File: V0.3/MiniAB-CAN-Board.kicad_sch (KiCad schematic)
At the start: 119 parts, among them J1 PC-FAN, J10 USB_B_Micro, J11 ENDSTOP1, J12 CAN, J13 ENDSTOP2, J14 PROBE, J2 PC-FAN, J3 HE-FAN, J4 TH0, J5 H0, J6 STEPPER, J7 NEOPIXEL, J8 I2C, J9 Conn_02x03_Top_Bottom, Q1 AO3400A, Q2 AO3400A, Q3 AON7418, U1 ADXL345BCCZ-RL7, U2 STM32F103C8Tx, U3 74LVC1G17, U4 LP5907MFX-3.3, U5 TMC2209-LA, U6 TPS54202DDC, U7 TCAN330, Y1 8MHz

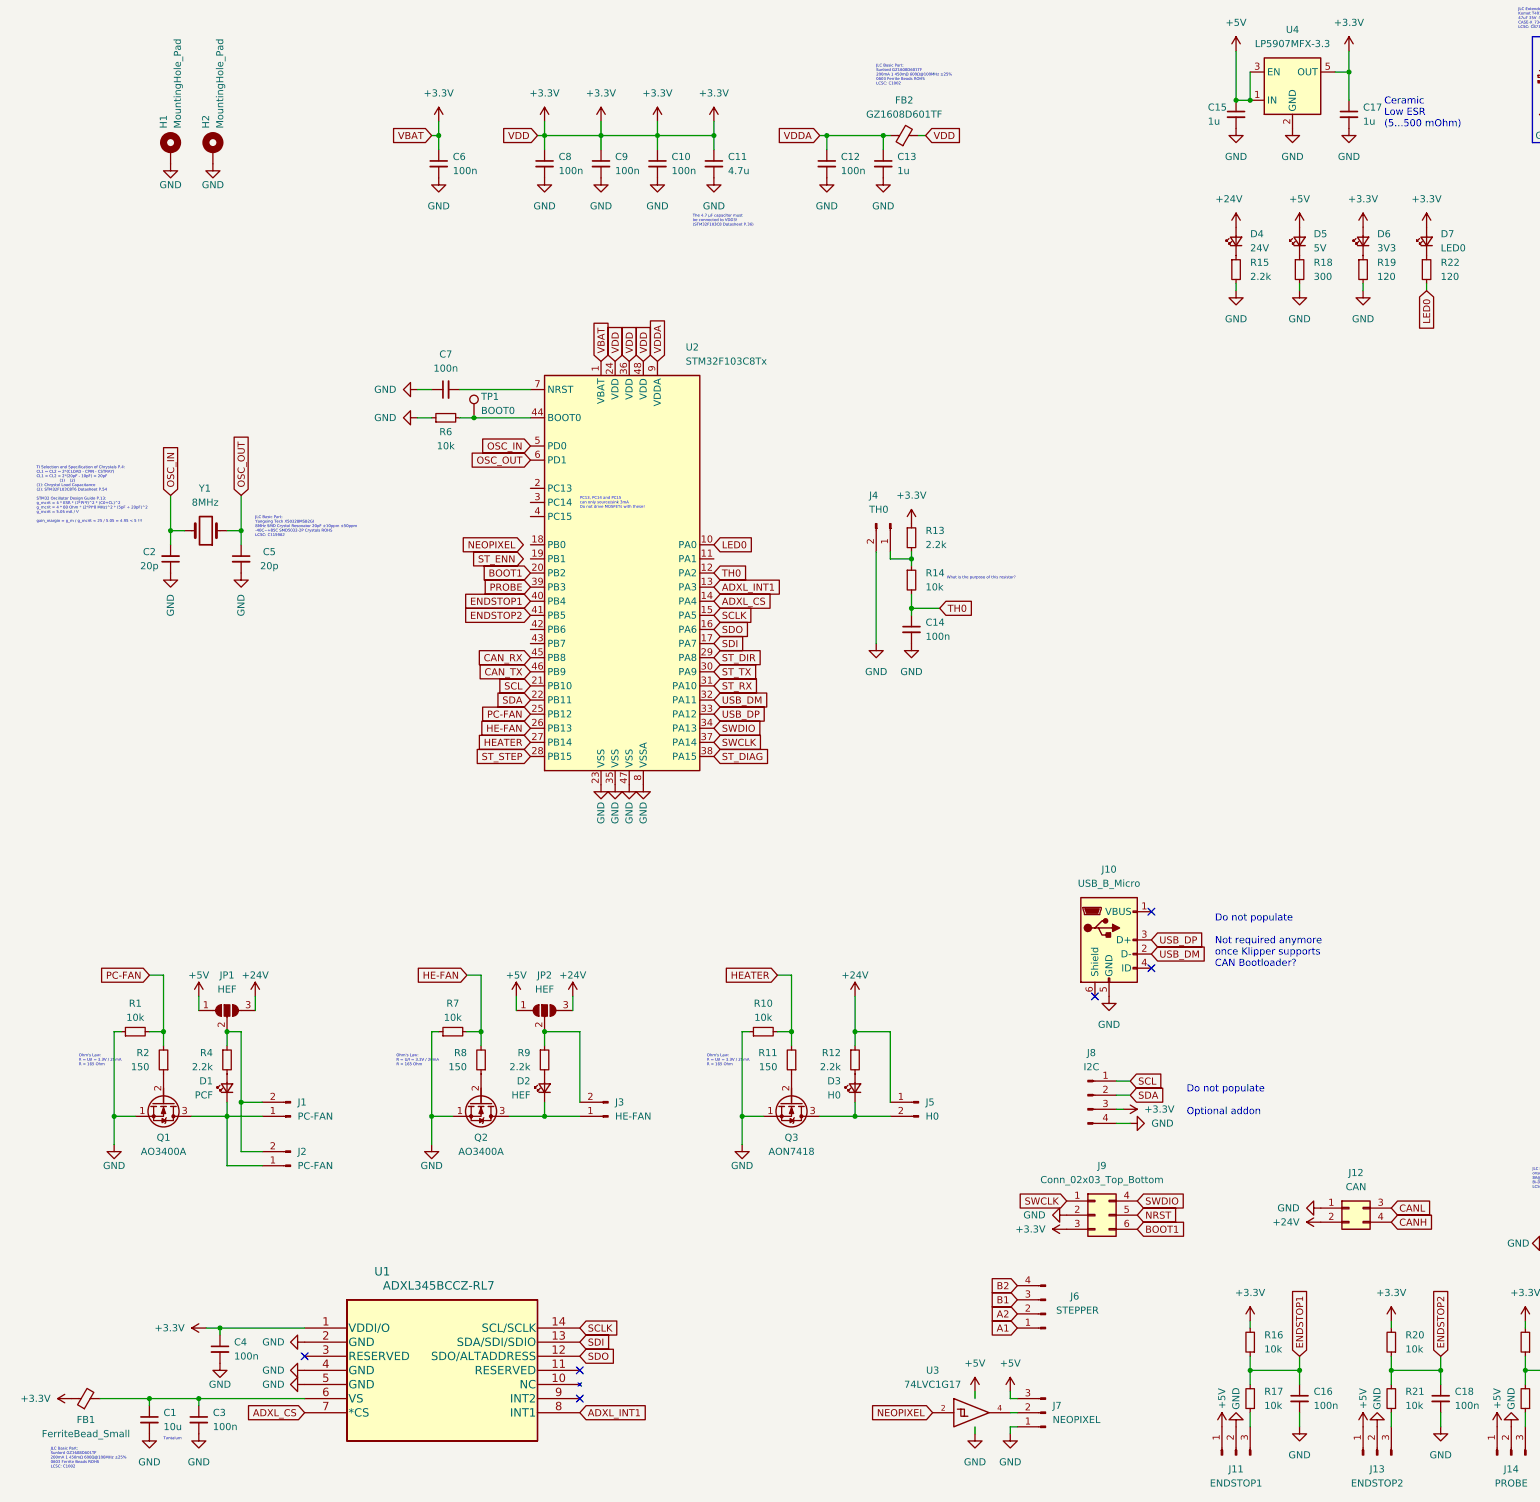
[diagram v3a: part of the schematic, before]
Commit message: Updated footprints to 0402 if possible
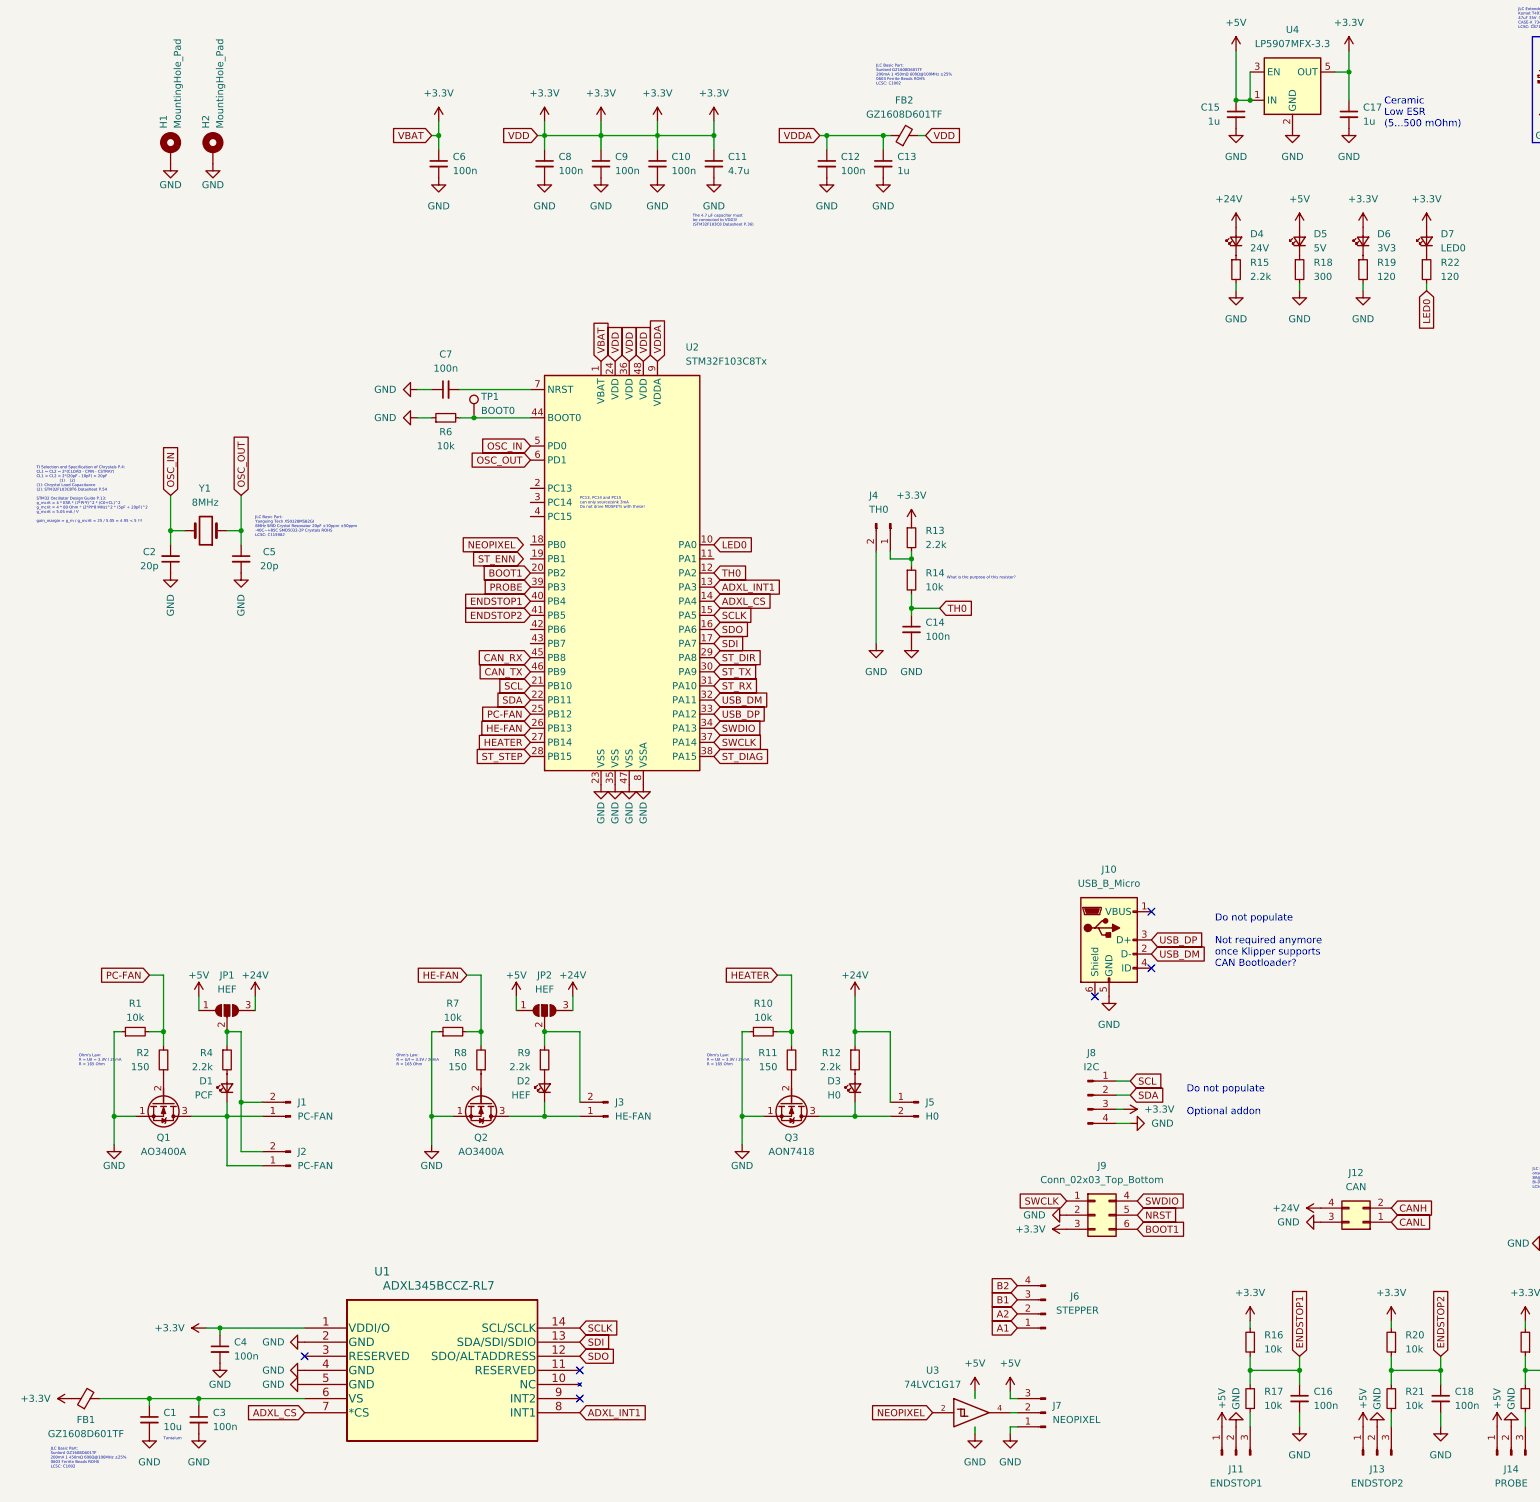
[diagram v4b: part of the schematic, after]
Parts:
- C10, C11, C12, C13, C14, C15, C16, C17, C18, C2, C20, C22, C23, C24, C26, C27, C28, C29, C3, C30, C33, C34, C35, C4, C40, C41, C43, C5, C6, C7, C8, C9: footprint Capacitor_SMD:C_0603_1608Metric -> Capacitor_SMD:C_0402_1005Metric
- D1, D2, D3, D4, D5, D6, D7: footprint LED_SMD:LED_0805_2012Metric -> LED_SMD:LED_0402_1005Metric
- D9: footprint LED_SMD:LED_0603_1608Metric -> LED_SMD:LED_0402_1005Metric
- FB1: value FerriteBead_Small -> GZ1608D601TF
- R1, R10, R11, R12, R13, R14, R15, R16, R17, R18, R19, R2, R20, R21, R22, R23, R24, R25, R26, R29, R34, R35, R36, R4, R6, R7, R8, R9: footprint Resistor_SMD:R_0603_1608Metric -> Resistor_SMD:R_0402_1005Metric
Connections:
- net +24V: now also J12.4 (Pin_4); no longer J12.2 (Pin_2)
- net CANH: now also J12.2 (Pin_2); no longer J12.4 (Pin_4)
- net CANL: now also J12.1 (Pin_1); no longer J12.3 (Pin_3)
- net GND: now also J12.3 (Pin_3); no longer J12.1 (Pin_1)
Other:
- moved on the sheet: J12

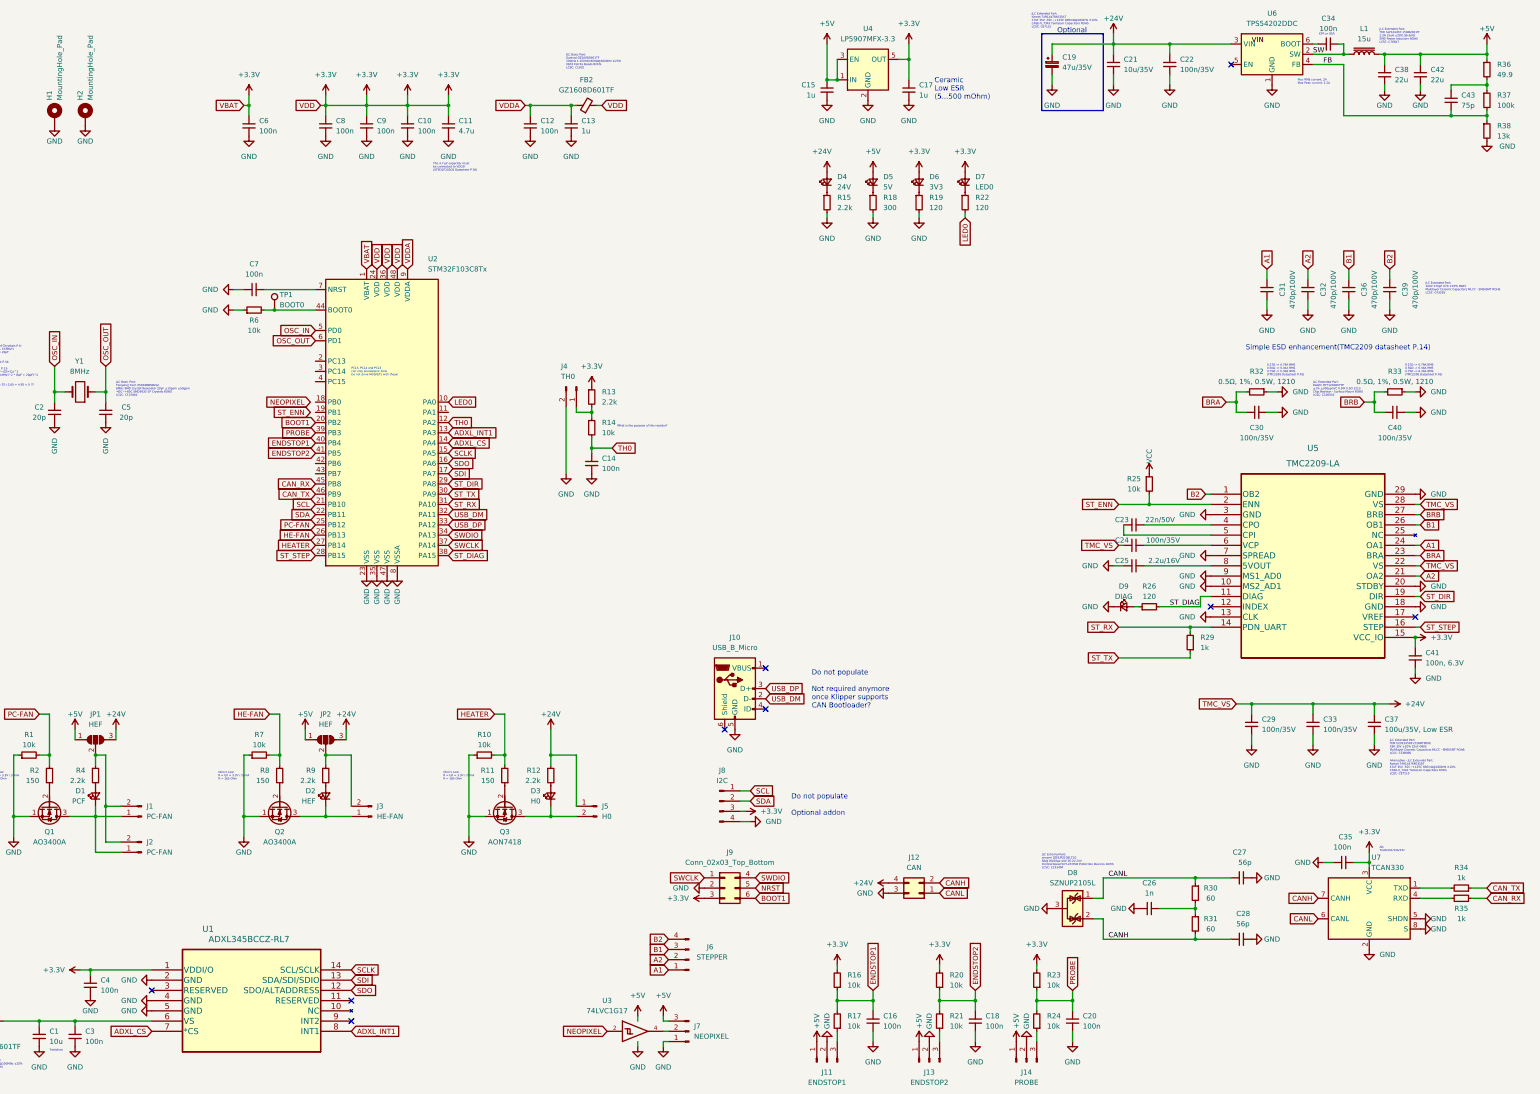
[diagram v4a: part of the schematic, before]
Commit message: TMC added to V0.3
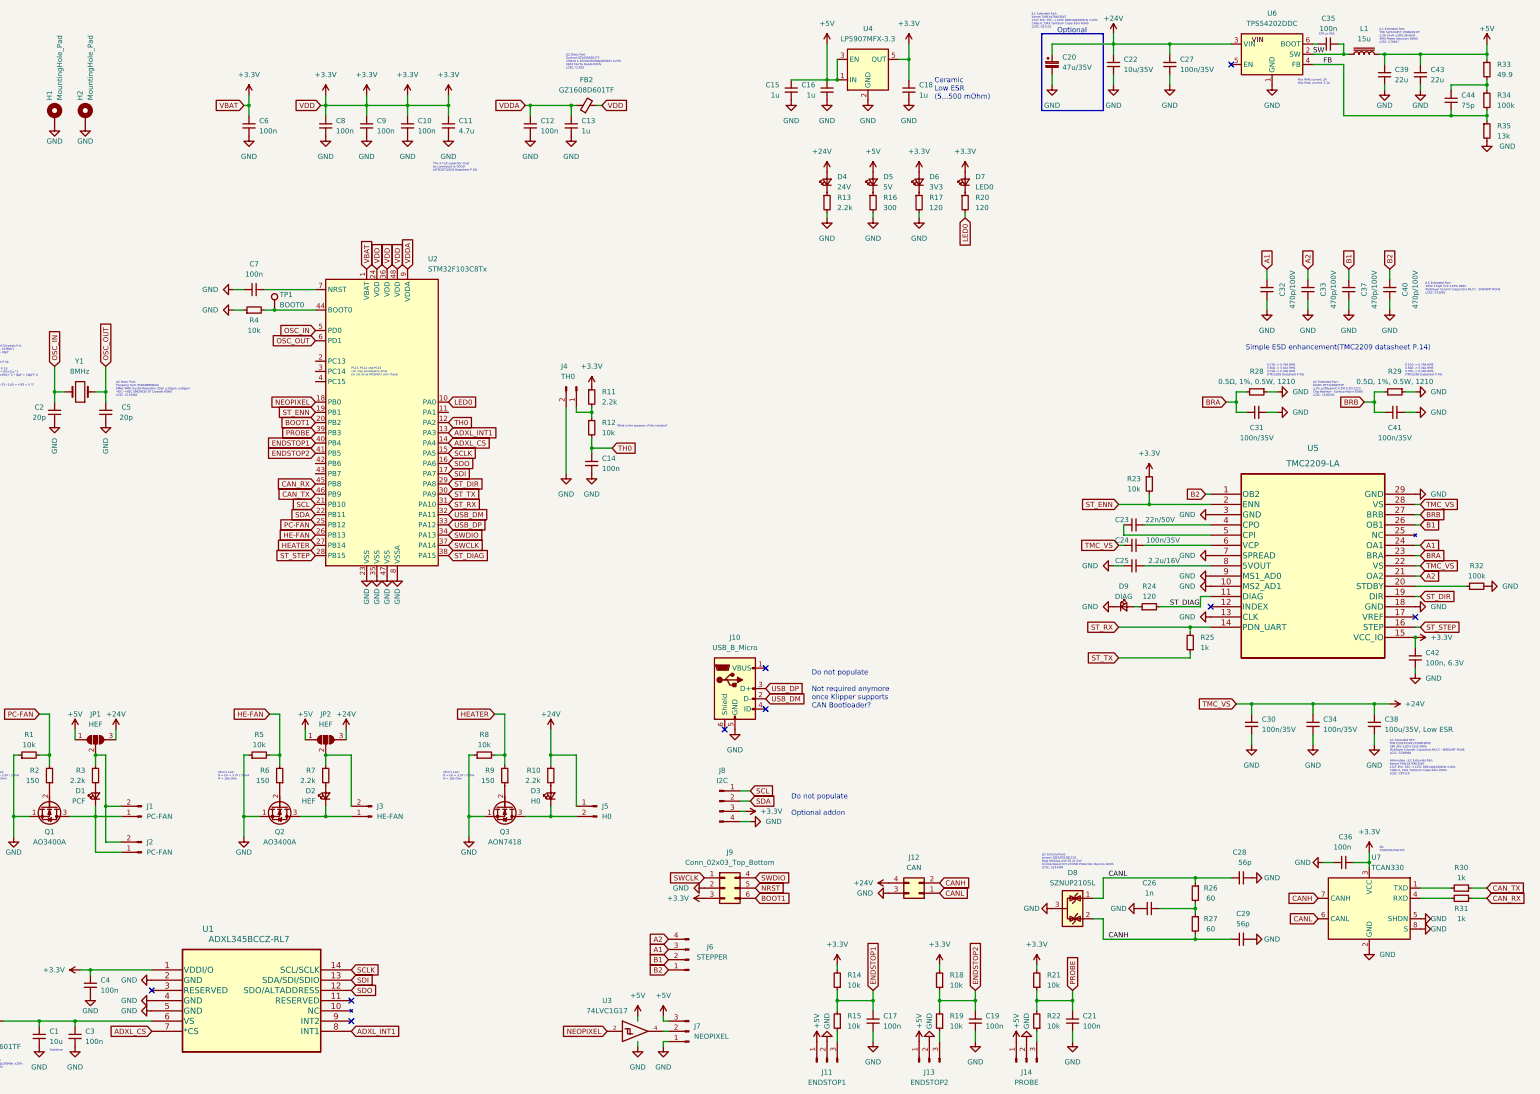
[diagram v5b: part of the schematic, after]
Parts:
- added C15: 1u, Capacitor_SMD:C_0402_1005Metric, symbol Device:C_Small
- added R32: 100k, Resistor_SMD:R_0402_1005Metric, symbol Device:R_Small
- renumbered C15 to C16, C16 to C17, C17 to C18, C18 to C19, C19 to C20, C20 to C21, C21 to C22, C22 to C27, C27 to C28, C28 to C29, C29 to C30, C30 to C31, C31 to C32, C32 to C33, C33 to C34, C34 to C35, C35 to C36, C36 to C37, C37 to C38, C38 to C39, C39 to C40, C40 to C41, C41 to C42, C42 to C43, C43 to C44, R12 to R10, R13 to R11, R14 to R12, R15 to R13, R16 to R14, R17 to R15, R18 to R16, R19 to R17, R20 to R18, R21 to R19, R22 to R20, R23 to R21, R24 to R22, R25 to R23, R26 to R24, R29 to R25, R30 to R26, R31 to R27, R32 to R28, R33 to R29, R4 to R3, R34 to R30, R35 to R31, R36 to R33, R37 to R34, R38 to R35, R6 to R4, R7 to R5, R8 to R6, R9 to R7, R10 to R8, R11 to R9
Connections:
- net +3V3: now also R23.1
- net +5V: now also C15.1; no longer R23.1
- net A1: now also J6.3 (Pin_3); no longer J6.1 (Pin_1)
- net A2: now also J6.4 (Pin_4); no longer J6.2 (Pin_2)
- net B1: now also J6.2 (Pin_2); no longer J6.3 (Pin_3)
- net B2: now also J6.1 (Pin_1); no longer J6.4 (Pin_4)
- net GND: now also C15.2, R32.2; no longer U5.20 (STDBY)
- net NEOPIXEL: now also U2.18 (PB0)
- net ST_ENN: now also U2.19 (PB1)
- new net: R32.1, U5.20 (STDBY)
